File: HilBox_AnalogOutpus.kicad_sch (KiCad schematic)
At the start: 64 parts, among them J1 Conn_01x02_Pin, J2 Conn_01x02_Pin, J3 Conn_01x02_Pin, J4 Conn_01x02_Pin, Q22 BC847BS, Q24 BC847BS, U2 MCP4822, U24 TLV272IS-13, U3 BU4S66G2-TR, U5 BU4S66G2-TR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

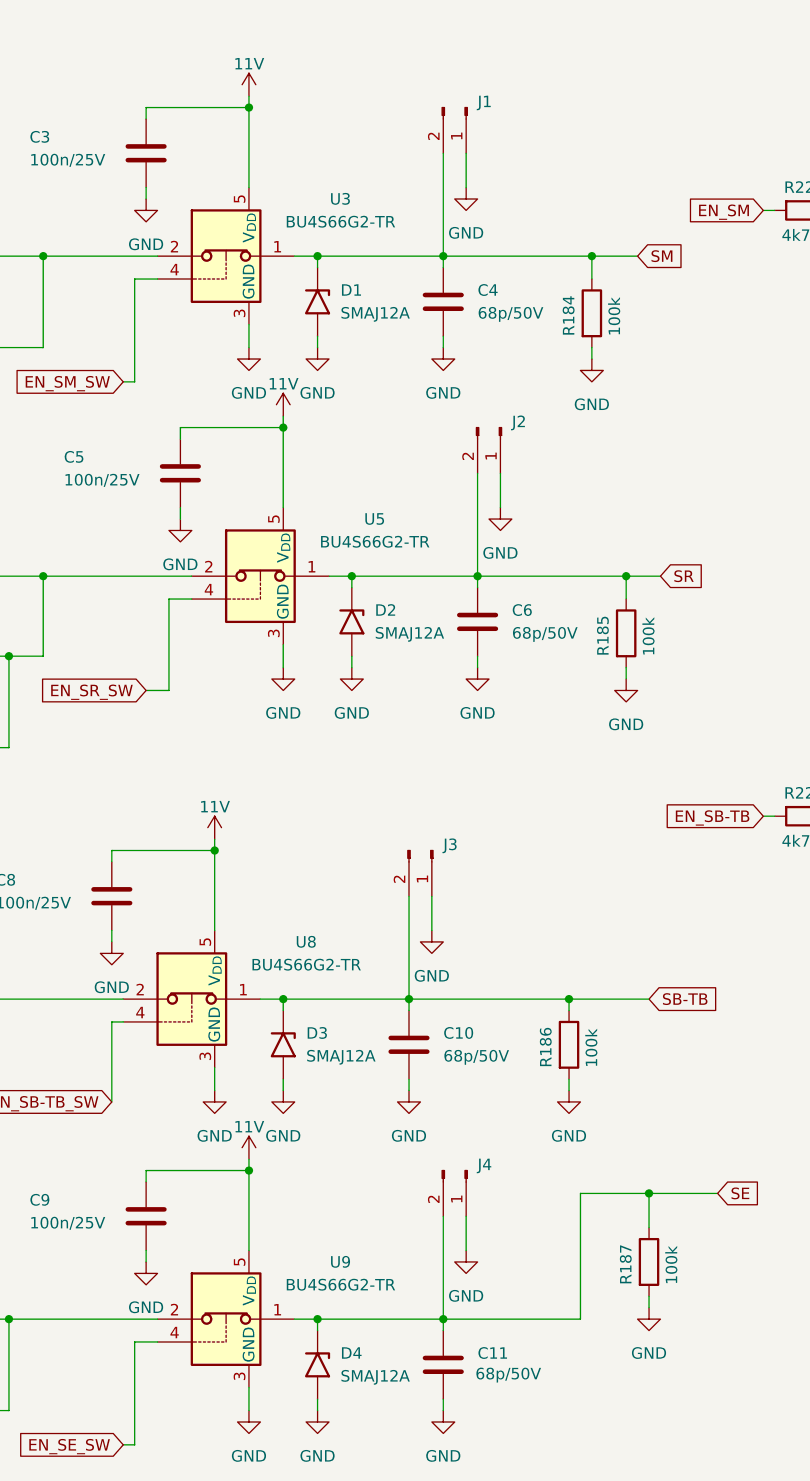
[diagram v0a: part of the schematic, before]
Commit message: Modification in half of target
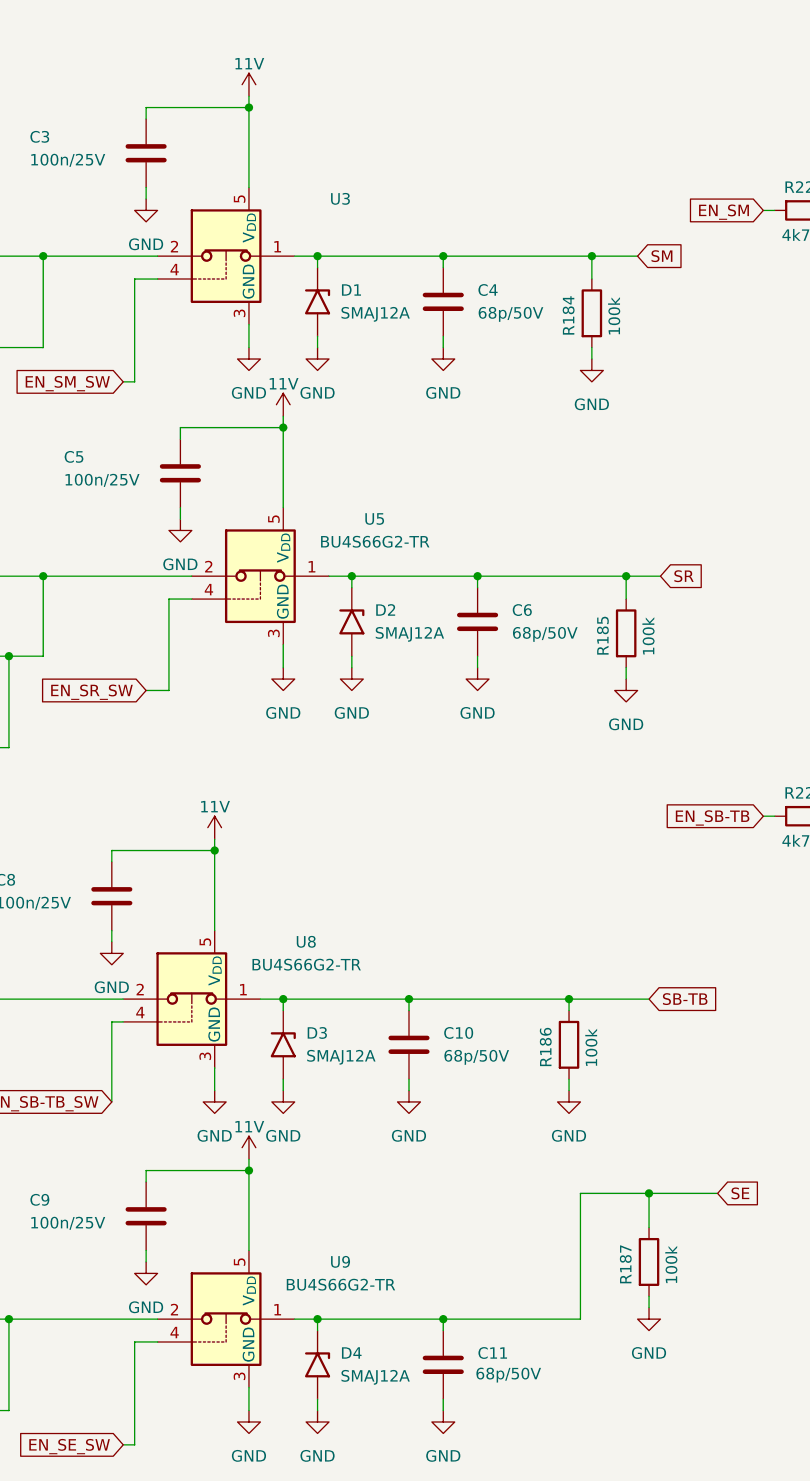
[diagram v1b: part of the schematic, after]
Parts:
- removed J1, J2, J3, J4: Conn_01x02_Pin, Connector_PinHeader_2.54mm:PinHeader_1x02_P2.54mm_Vertical, symbol Connector:Conn_01x02_Pin

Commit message: Layout 90% done
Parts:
- removed C10, C11: 68p/50V, Capacitor_SMD:C_0402_1005Metric, symbol Device:C
- removed C108, C109: 10p, Capacitor_SMD:C_0402_1005Metric, symbol Device:C
- removed C12, C3, C5, C7, C8, C9: 100n/25V, Capacitor_SMD:C_0402_1005Metric, symbol Device:C
- removed D3, D4: SMAJ12A, Diode_SMD:D_SMA, symbol Diode:SMAJ12A
- removed Q22, Q24: BC847BS, Package_TO_SOT_SMD:SOT-363_SC-70-6, symbol Transistor_BJT:BC847BS
- removed R10, R8, R9: 0R/1%, Resistor_SMD:R_0603_1608Metric, symbol Device:R
- removed R11, R12: 2k2/1%, Resistor_SMD:R_0603_1608Metric, symbol Device:R
- removed R13, R14: 4k7/1%, Resistor_SMD:R_0603_1608Metric, symbol Device:R
- removed R186, R187: 100k, Resistor_SMD:R_0603_1608Metric, symbol Device:R
- removed R222, R223, R226, R231: 4k7/1%, Resistor_SMD:R_0402_1005Metric, symbol Device:R
- removed R224, R225, R227, R228, R229, R230, R232, R233: 10k, Resistor_SMD:R_0402_1005Metric, symbol Device:R
- removed U3, U5, U8, U9: BU4S66G2-TR, Package_TO_SOT_SMD:SOT-23-5, symbol Analog_Switch:TMUX1102DCK
- removed U6: MCP4822, Package_SO:SOIC-8_3.9x4.9mm_P1.27mm, symbol Analog_DAC:MCP4822
- removed U7: TLV272IS-13, Package_SO:VSSOP-8_3x3mm_P0.65mm, symbol Amplifier_Operational:MCP6002-xMC
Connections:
- net SM: now also C106.2, R3.1, U24.1
- net SR: now also C107.2, R6.1, U24.7
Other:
- moved on the sheet: C4, C6, D1, D2, R184, R185
